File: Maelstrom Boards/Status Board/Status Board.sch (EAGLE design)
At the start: 28 parts, among them IC1 LM555D, P1 39-30-04, Q1 310mA/60V/1.6Ω

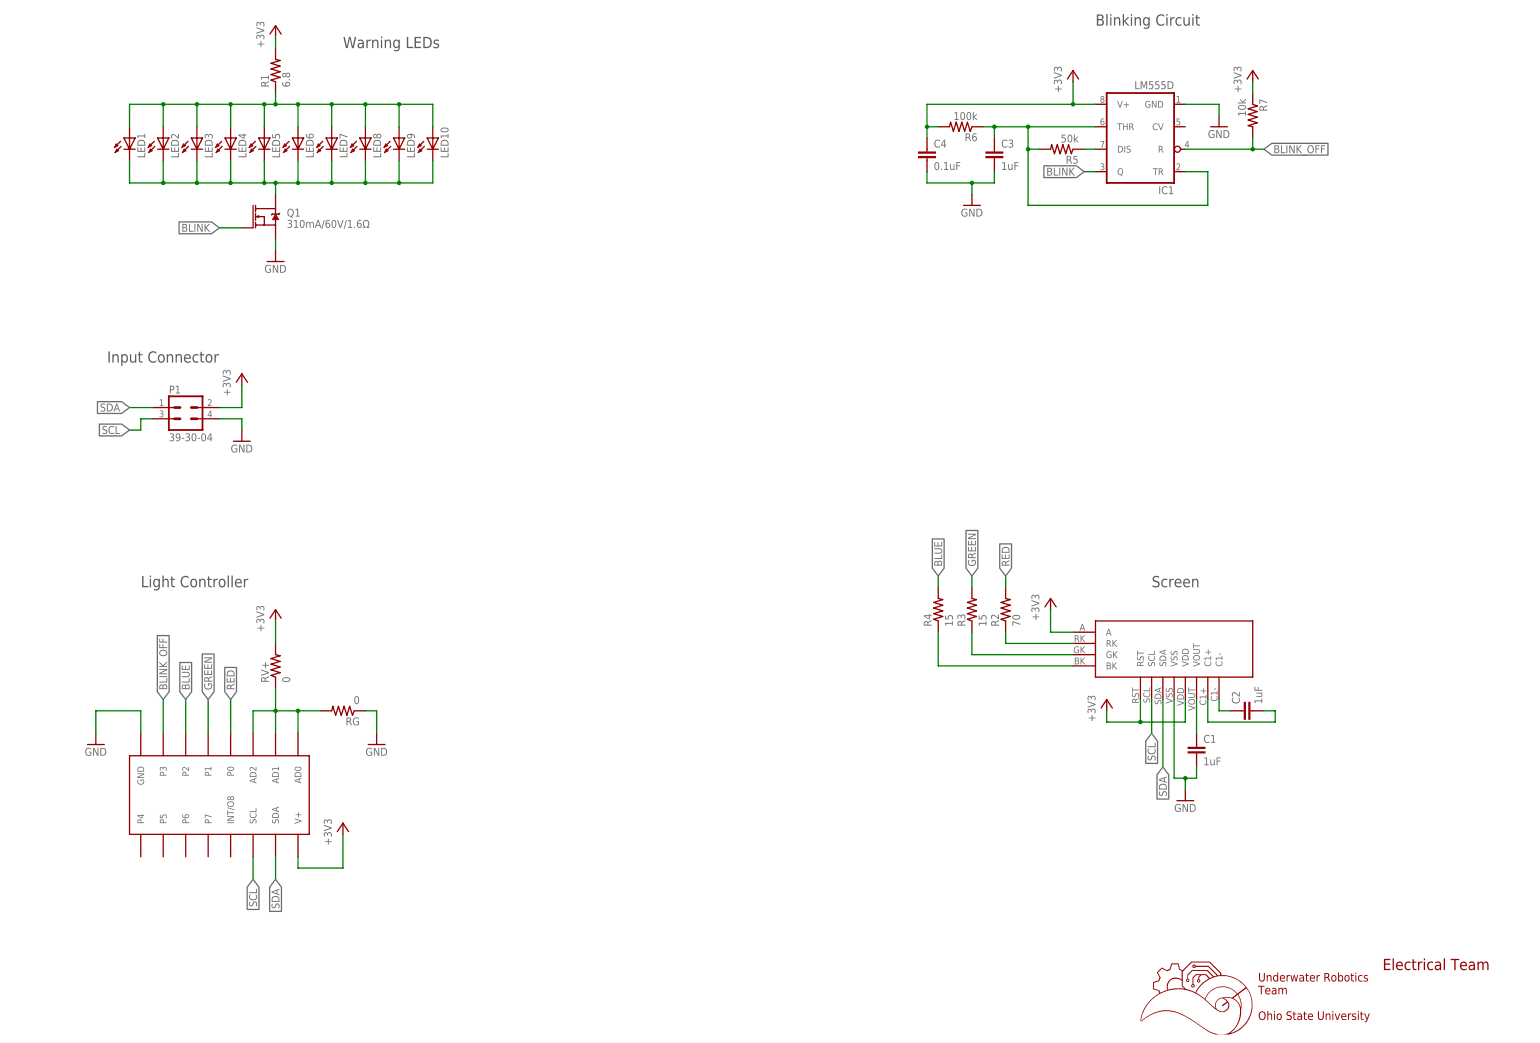
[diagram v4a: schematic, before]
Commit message: Adding caps and fixing screen
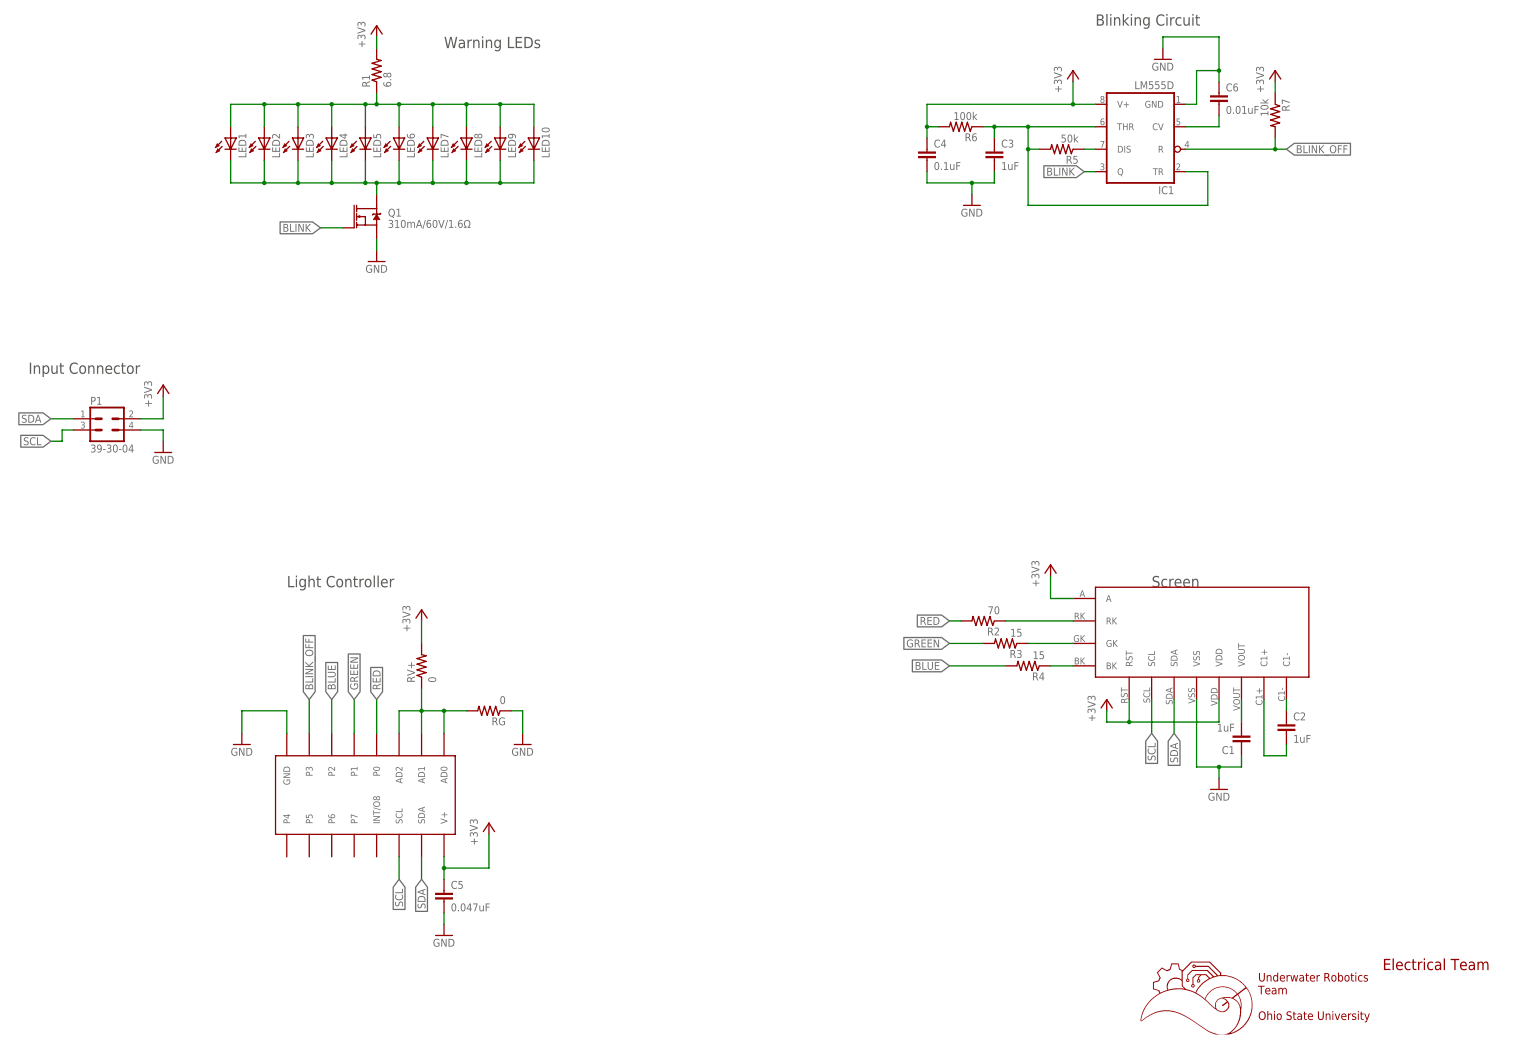
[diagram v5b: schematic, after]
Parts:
- added C5: 0.047uF, rcl:C-EUC0603
- added C6: 0.01uF, rcl:C-EUC0603
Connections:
- new net N$8: C6.2, IC1.CV
- net +3V3: now also C5.1
- net GND: now also C1.1, C5.2, C6.1; no longer C1.2
- net N$3: now also C1.2; no longer C1.1
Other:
- moved on the sheet: C1, C2, LED1, LED10, LED2, LED3, LED4, LED5, LED6, LED7, LED8, LED9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

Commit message: Updating status schematic
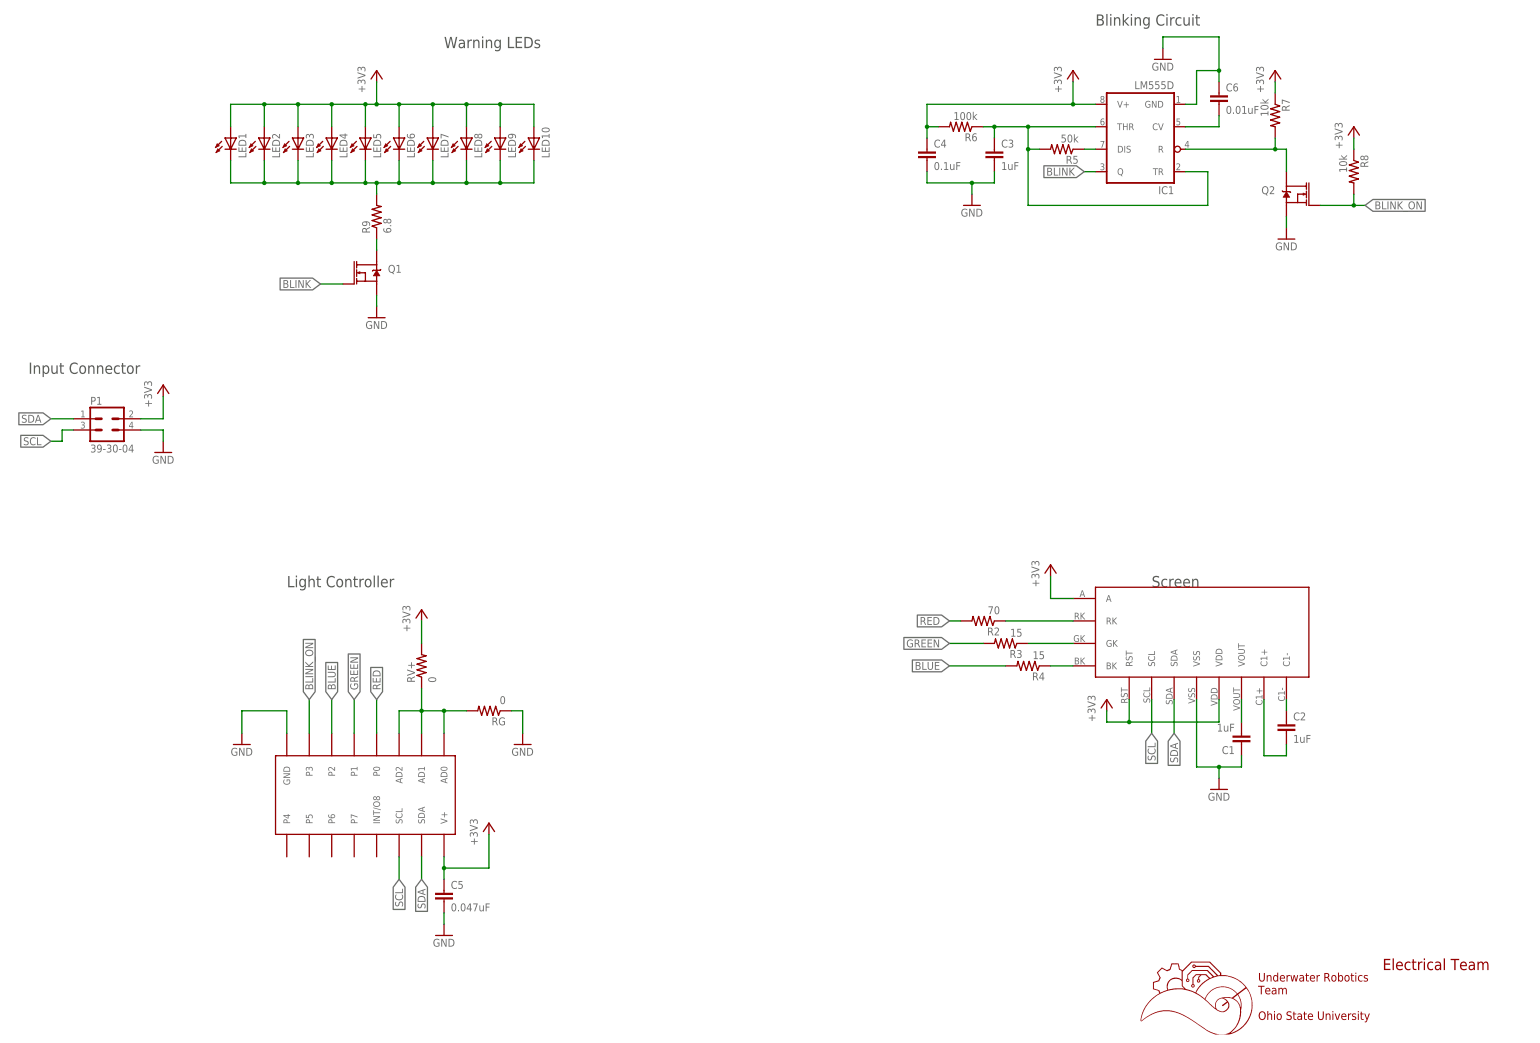
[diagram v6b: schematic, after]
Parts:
- removed R1: 6.8, rcl:R-US_R0603
- added Q2: 310mA/60V/1.6Ω, SparkFun-DiscreteSemi:MOSFET-NCH-2N7002PW
- added R8: 10k, rcl:R-US_R0603
- added R9: 6.8, rcl:R-US_R0603
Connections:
- removed net N$11: LED1.A, LED10.A, LED2.A, LED3.A, LED4.A, LED5.A, LED6.A, LED7.A, LED8.A, LED9.A, R1.1
- new net BLINK_ON: Q2.G, R8.2, U$2.P3
- new net N$12: Q1.D, R9.1
- net +3V3: now also LED1.A, LED10.A, LED2.A, LED3.A, LED4.A, LED5.A, LED6.A, LED7.A, LED8.A, LED9.A, R8.1; no longer R1.2
- net BLINK_OFF: now also Q2.D; no longer U$2.P3
- net GND: now also Q2.S
- net N$20: now also R9.2; no longer Q1.D
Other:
- moved on the sheet: Q1

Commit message: Final changes before order
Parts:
- C5: value 0.047uF -> 47nF
- C6: value 0.01uF -> 10nF
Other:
- note added: "Must be > .25W"
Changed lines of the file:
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@@
 <part name="Q1" library="SparkFun-DiscreteSemi" library_urn="urn:adsk.eagle:library:514" deviceset="MOSFET-NCH" device="-2N7002PW" package3d_urn="urn:adsk.eagle:package:38456/1" value="310mA/60V/1.6Ω"/>
 <part name="GND3" library="supply1" library_urn="urn:adsk.eagle:library:371" deviceset="GND" device=""/>
-<part name="C5" library="rcl" library_urn="urn:adsk.eagle:library:334" deviceset="C-EU" device="C0603" package3d_urn="urn:adsk.eagle:package:23616/2" value="0.047uF"/>
+<part name="C5" library="rcl" library_urn="urn:adsk.eagle:library:334" deviceset="C-EU" device="C0603" package3d_urn="urn:adsk.eagle:package:23616/2" value="47nF"/>
 <part name="GND8" library="supply1" library_urn="urn:adsk.eagle:library:371" deviceset="GND" device=""/>
-<part name="C6" library="rcl" library_urn="urn:adsk.eagle:library:334" deviceset="C-EU" device="C0603" package3d_urn="urn:adsk.eagle:package:23616/2" value="0.01uF"/>
+<part name="C6" library="rcl" library_urn="urn:adsk.eagle:library:334" deviceset="C-EU" device="C0603" package3d_urn="urn:adsk.eagle:package:23616/2" value="10nF"/>
 <part name="Q2" library="SparkFun-DiscreteSemi" library_urn="urn:adsk.eagle:library:514" deviceset="MOSFET-NCH" device="-2N7002PW" package3d_urn="urn:adsk.eagle:package:38456/1" value="310mA/60V/1.6Ω"/>
 <part name="R8" library="rcl" library_urn="urn:adsk.eagle:library:334" deviceset="R-US_" device="R0603" package3d_urn="urn:adsk.eagle:package:23555/2" value="10k"/>
@@
 <text x="96.52" y="106.68" size="2.54" layer="97">Light Controller</text>
 <text x="38.1" y="154.94" size="2.54" layer="97">Input Connector</text>
+<text x="127" y="190.5" size="1.778" layer="97">Must be &gt; .25W</text>
 </plain>
 <instances>
